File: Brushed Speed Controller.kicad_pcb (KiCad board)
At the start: 2 copper layers, 80.6 x 71.1 mm, 22 parts, among them J1 Input, J2 Output, U1 TC4427, U2 TC4427, U3 SQJ500AEP-T1_GE3, U4 LM7805, U5 SQJ500AEP-T1_GE3

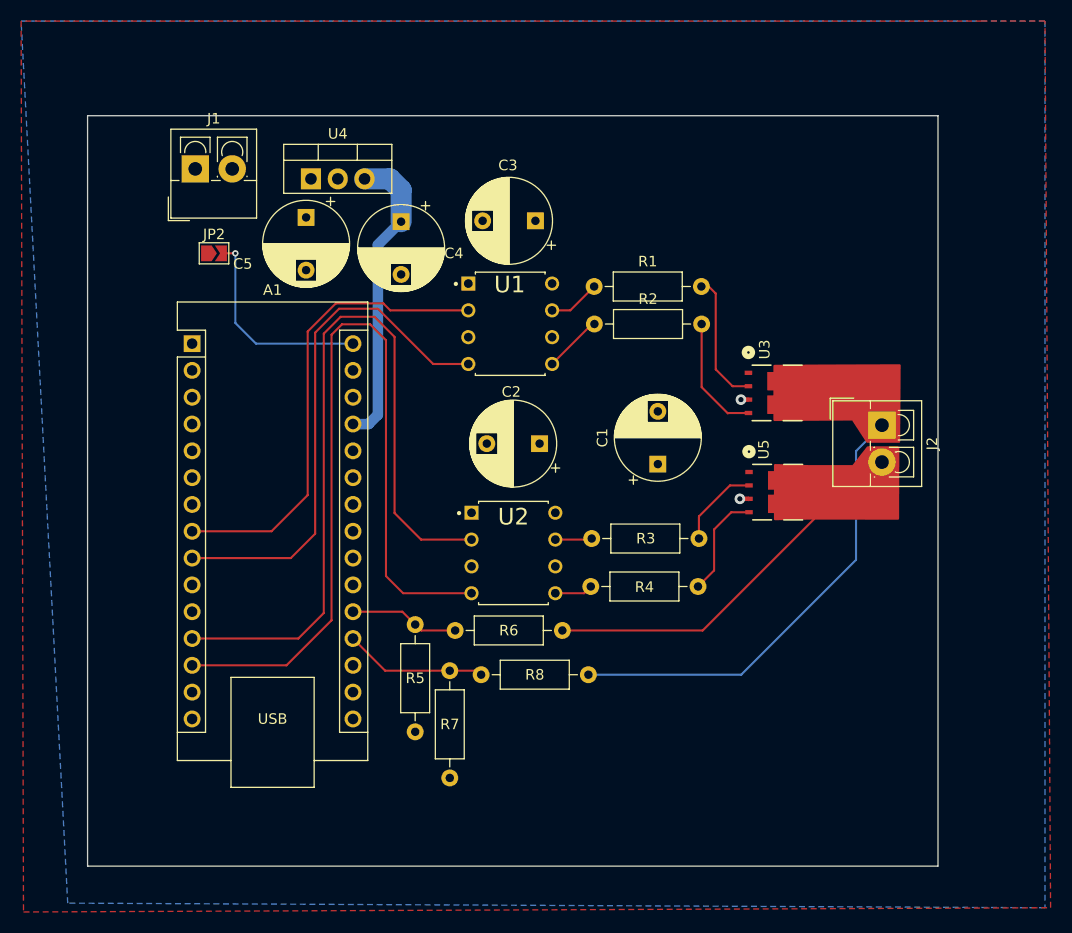
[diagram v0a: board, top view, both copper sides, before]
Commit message: Added bigger terminals
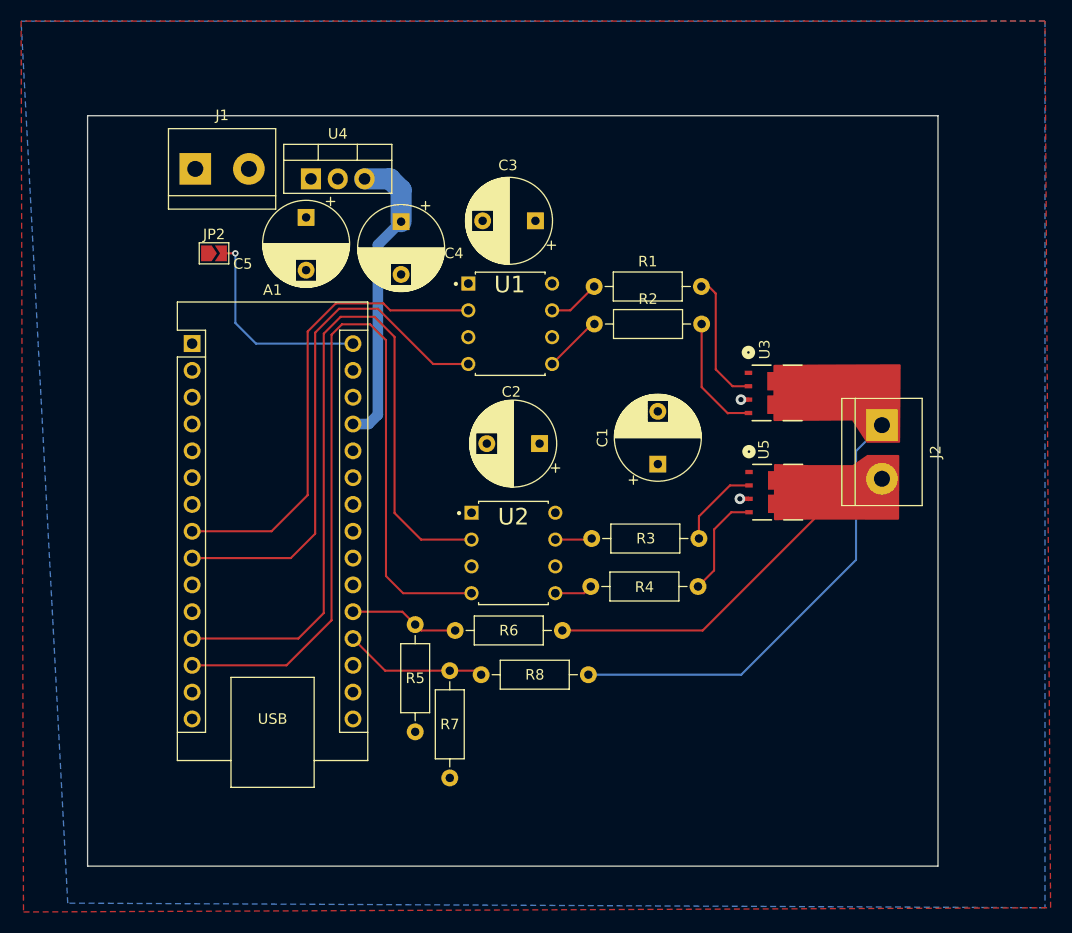
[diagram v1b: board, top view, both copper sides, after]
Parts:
- J1, J2: footprint TerminalBlock_4Ucon:TerminalBlock_4Ucon_1x02_P3.50mm_Vertical -> TerminalBlock:TerminalBlock_bornier-2_P5.08mm
